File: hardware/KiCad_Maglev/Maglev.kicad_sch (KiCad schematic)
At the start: 32 parts, among them J1 USB_C_Receptacle, J2 691103110002, J3 61300621121, J4 61300821121, U1 WE-TVS-82400102, U2 ESP32-C3

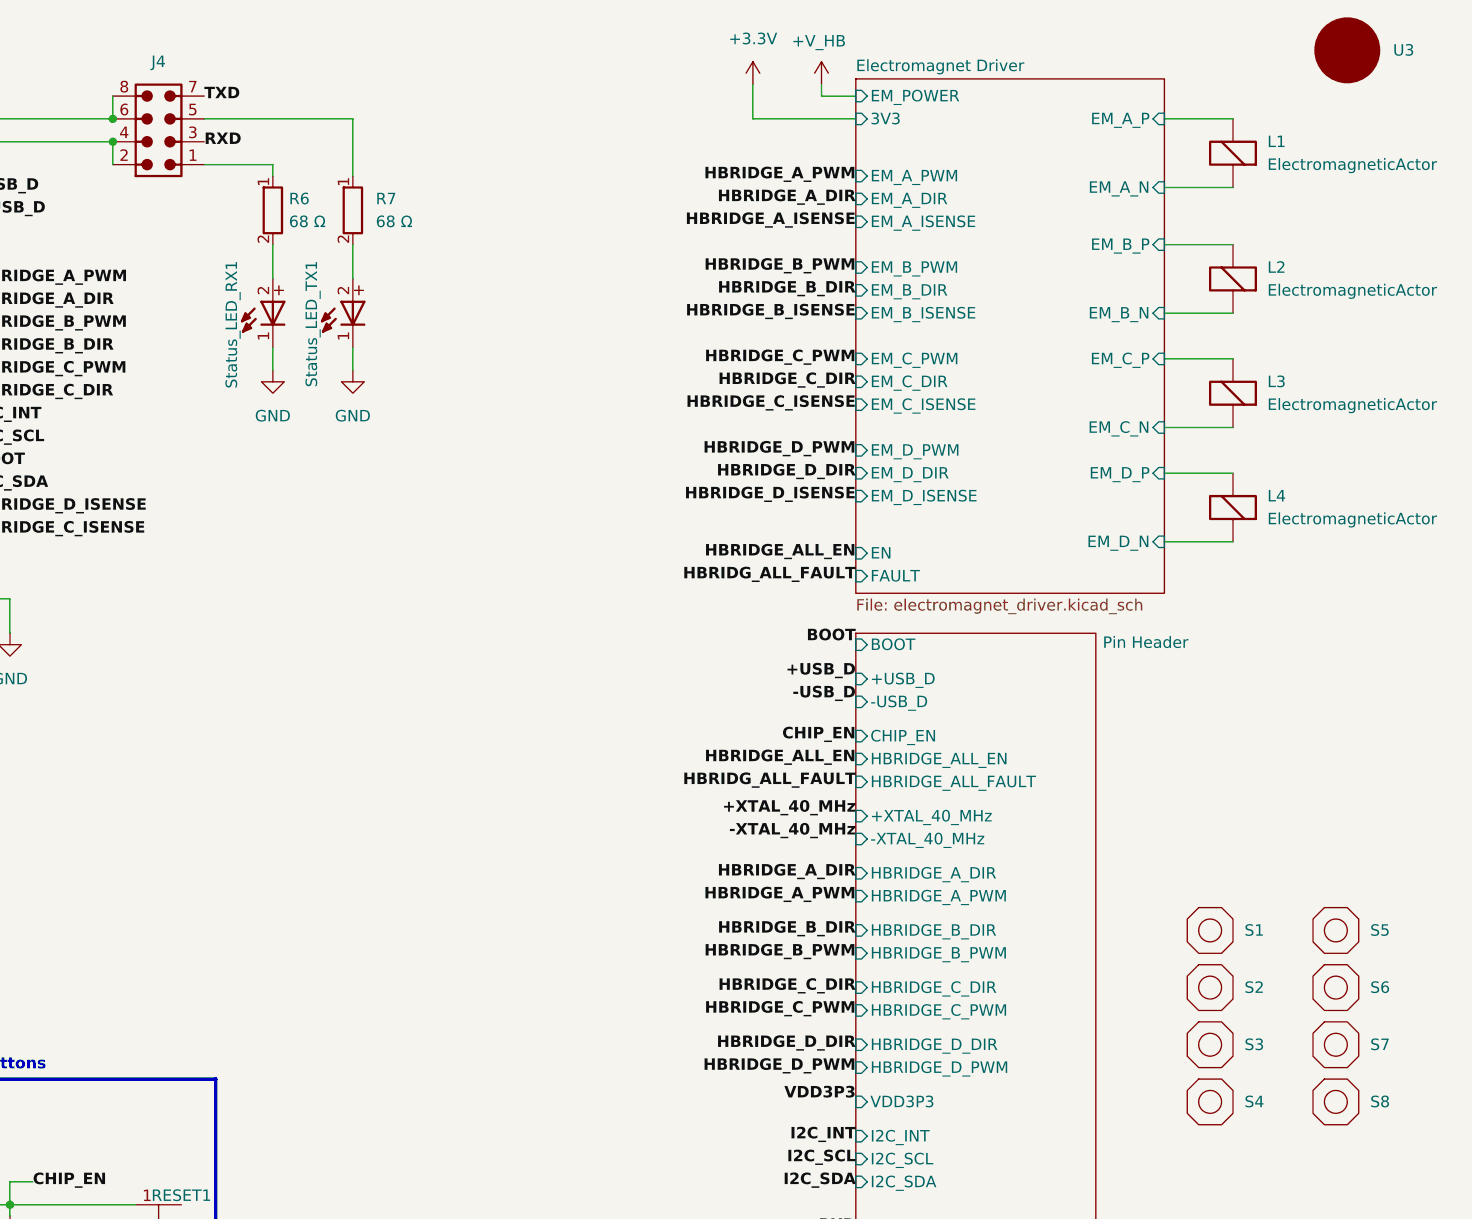
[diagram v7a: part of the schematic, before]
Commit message: Route power PCB and implement board-to-board connector
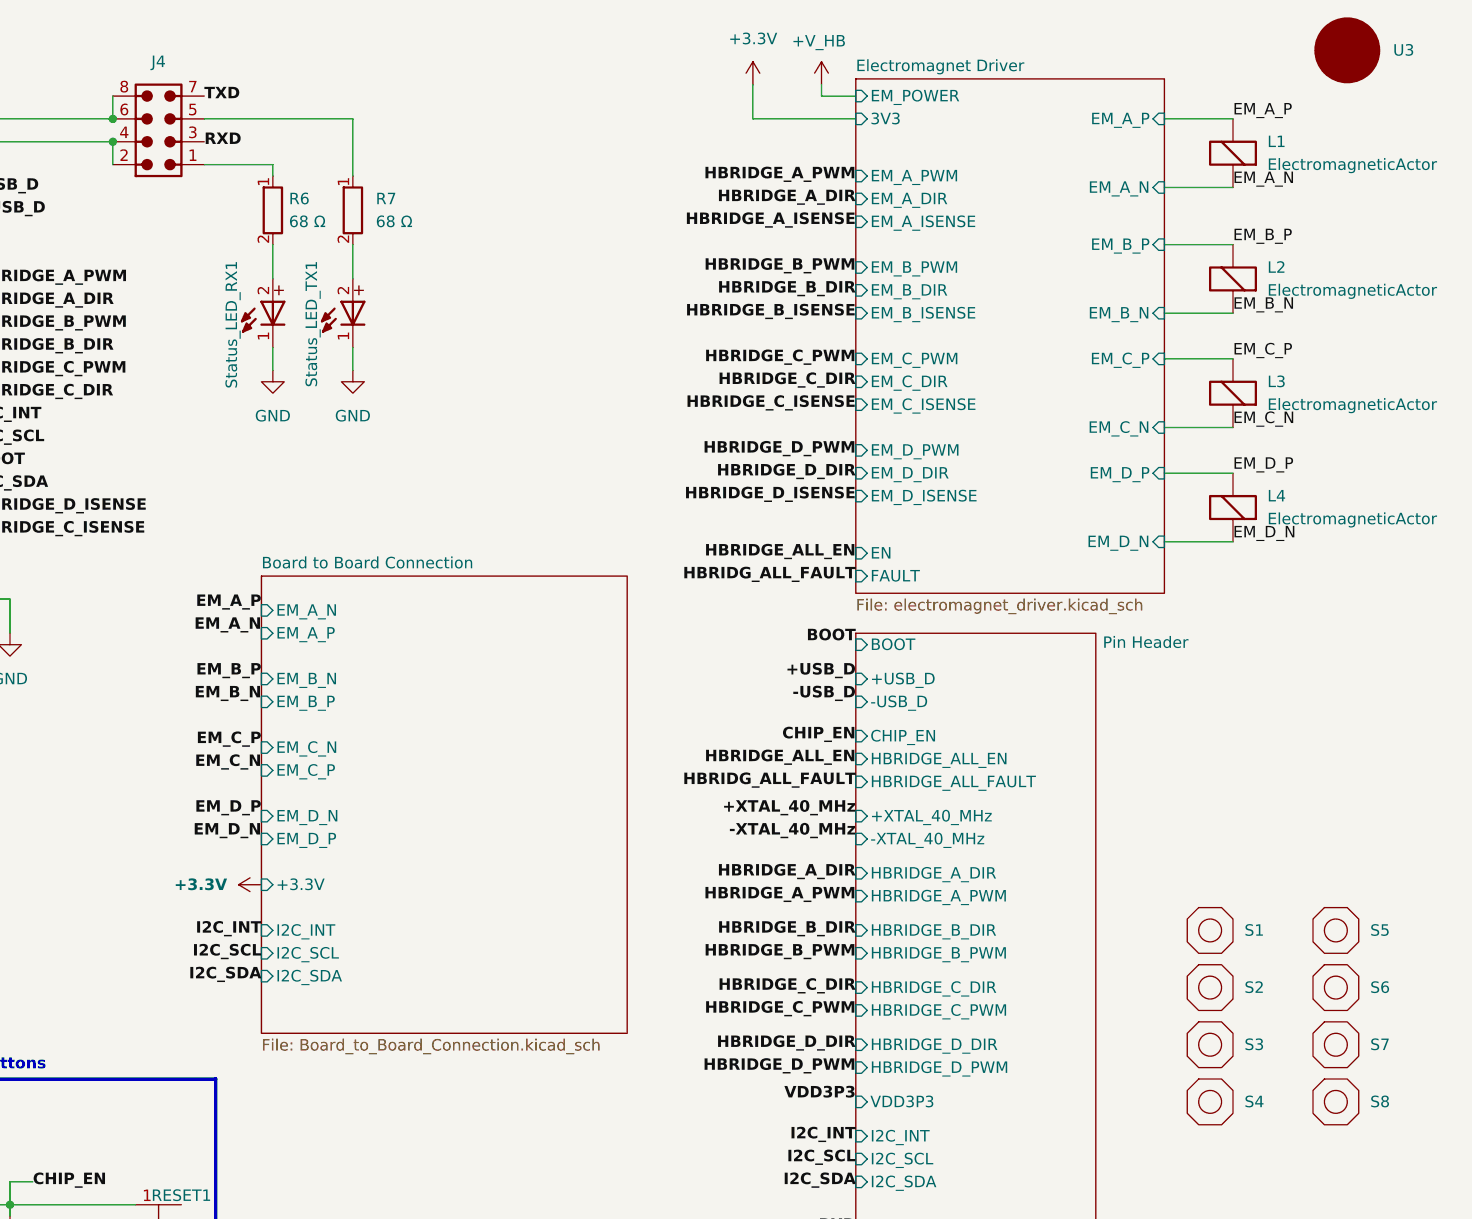
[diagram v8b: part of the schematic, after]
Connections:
- net Electromagnet Driver/EM_A_N renamed EM_A_N
- net Electromagnet Driver/EM_A_P renamed EM_A_P
- net Electromagnet Driver/EM_B_N renamed EM_B_N
- net Electromagnet Driver/EM_B_P renamed EM_B_P
- net Electromagnet Driver/EM_C_N renamed EM_C_N
- net Electromagnet Driver/EM_C_P renamed EM_C_P
- net Electromagnet Driver/EM_D_N renamed EM_D_N
- net Electromagnet Driver/EM_D_P renamed EM_D_P
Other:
- added sheet Board to Board Connection (Board_to_Board_Connection.kicad_sch)
